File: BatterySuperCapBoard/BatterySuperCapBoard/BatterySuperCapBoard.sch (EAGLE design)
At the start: 18 parts, among them X1 ESQ-126-38-G-D, X2 WEIDMULLER

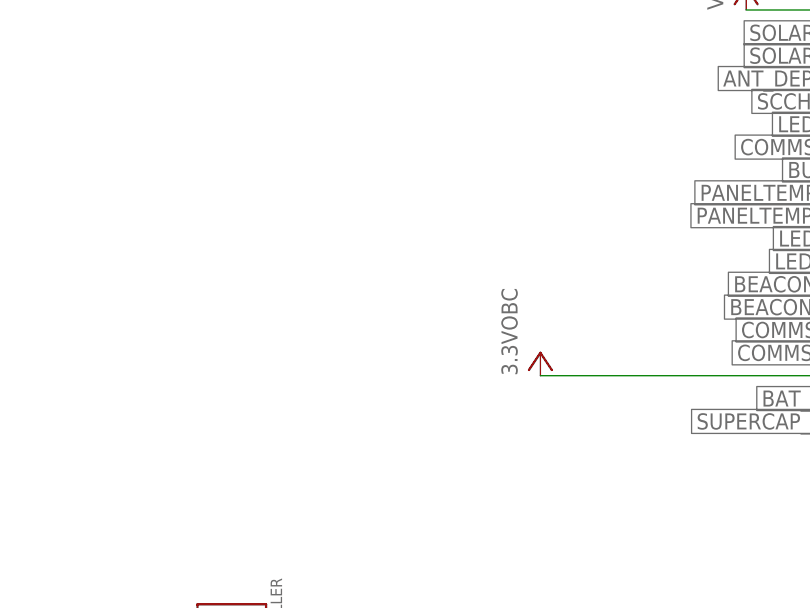
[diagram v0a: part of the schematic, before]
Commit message: supercap battery board added
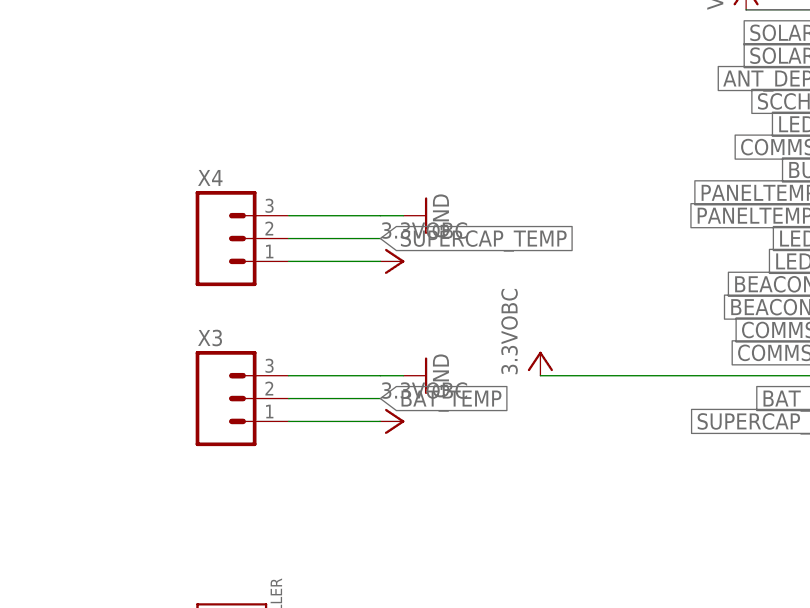
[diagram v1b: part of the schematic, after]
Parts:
- added X3, X4: (no value), OSSI:M03PTH
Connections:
- net 3.3VOBC: now also X3.1, X4.1
- net BAT_TEMP: now also X3.2
- net GND: now also X3.3, X4.3
- net SUPERCAP_TEMP: now also X4.2
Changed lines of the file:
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@@
 <part name="H15" library="OSSI" deviceset="MOUNT-PAD-ROUND" device="3.2"/>
 <part name="H16" library="OSSI" deviceset="MOUNT-PAD-ROUND" device="3.2"/>
+<part name="X3" library="OSSI" deviceset="M03" device="PTH"/>
+<part name="X4" library="OSSI" deviceset="M03" device="PTH"/>
+<part name="3.3VOBC1" library="OSSI" deviceset="3.3VOBC" device=""/>
+<part name="3.3VOBC2" library="OSSI" deviceset="3.3VOBC" device=""/>
+<part name="GND1" library="OSSI" deviceset="GND" device=""/>
+<part name="GND2" library="OSSI" deviceset="GND" device=""/>
 </parts>
 <sheets>
@@
 <instance part="H15" gate="G$1" x="116.84" y="88.9"/>
 <instance part="H16" gate="G$1" x="134.62" y="86.36"/>
+<instance part="X3" gate="G$1" x="116.84" y="137.16"/>
+<instance part="X4" gate="G$1" x="116.84" y="154.94"/>
+<instance part="3.3VOBC1" gate="G$1" x="134.62" y="134.62" rot="R270"/>
+<instance part="3.3VOBC2" gate="G$1" x="134.62" y="152.4" rot="R270"/>
+<instance part="GND1" gate="1" x="139.7" y="157.48" rot="R90"/>
+<instance part="GND2" gate="1" x="139.7" y="139.7" rot="R90"/>
 </instances>
 <busses>
@@
 <wire x1="185.42" y1="132.08" x2="193.04" y2="132.08" width="0.1524" layer="91"/>
 </segment>
+<segment>
+<pinref part="X4" gate="G$1" pin="3"/>
+<wire x1="124.46" y1="157.48" x2="134.62" y2="157.48" width="0.1524" layer="91"/>
+<pinref part="GND1" gate="1" pin="GND"/>
+<wire x1="134.62" y1="157.48" x2="137.16" y2="157.48" width="0.1524" layer="91"/>
+</segment>
+<segment>
+<pinref part="X3" gate="G$1" pin="3"/>
+<wire x1="124.46" y1="139.7" x2="134.62" y2="139.7" width="0.1524" layer="91"/>
+<pinref part="GND2" gate="1" pin="GND"/>
+<wire x1="134.62" y1="139.7" x2="137.16" y2="139.7" width="0.1524" layer="91"/>
+</segment>
 </net>
 <net name="3.3VOBC" class="0">
@@
 <pinref part="3.3VOBC12" gate="G$1" pin="3.3VOBC"/>
 <wire x1="208.28" y1="139.7" x2="251.46" y2="139.7" width="0.1524" layer="91"/>
+</segment>
+<segment>
+<pinref part="X4" gate="G$1" pin="1"/>
+<wire x1="124.46" y1="152.4" x2="134.62" y2="152.4" width="0.1524" layer="91"/>
+<pinref part="3.3VOBC2" gate="G$1" pin="3.3VOBC"/>
+</segment>
+<segment>
+<pinref part="X3" gate="G$1" pin="1"/>
+<wire x1="124.46" y1="134.62" x2="134.62" y2="134.62" width="0.1524" layer="91"/>
+<pinref part="3.3VOBC1" gate="G$1" pin="3.3VOBC"/>
 </segment>
 </net>
@@
 <label x="190.5" y="137.16" size="1.778" layer="95" rot="R180" xref="yes"/>
 </segment>
+<segment>
+<pinref part="X3" gate="G$1" pin="2"/>
+<wire x1="124.46" y1="137.16" x2="134.62" y2="137.16" width="0.1524" layer="91"/>
+<label x="134.62" y="137.16" size="1.778" layer="95" xref="yes"/>
+</segment>
 </net>
 <net name="SUPERCAP_TEMP" class="0">
@@
 <label x="190.5" y="134.62" size="1.778" layer="95" rot="R180" xref="yes"/>
 </segment>
-</net>
+<segment>
+<pinref part="X4" gate="G$1" pin="2"/>
+<wire x1="124.46" y1="154.94" x2="134.62" y2="154.94" width="0.1524" layer="91"/>
+<label x="134.62" y="154.94" size="1.778" layer="95" xref="yes"/>
+</segment>
+</net>
